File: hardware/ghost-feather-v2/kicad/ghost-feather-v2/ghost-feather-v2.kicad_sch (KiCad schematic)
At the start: 10 parts, among them U1 STM32F722RETx

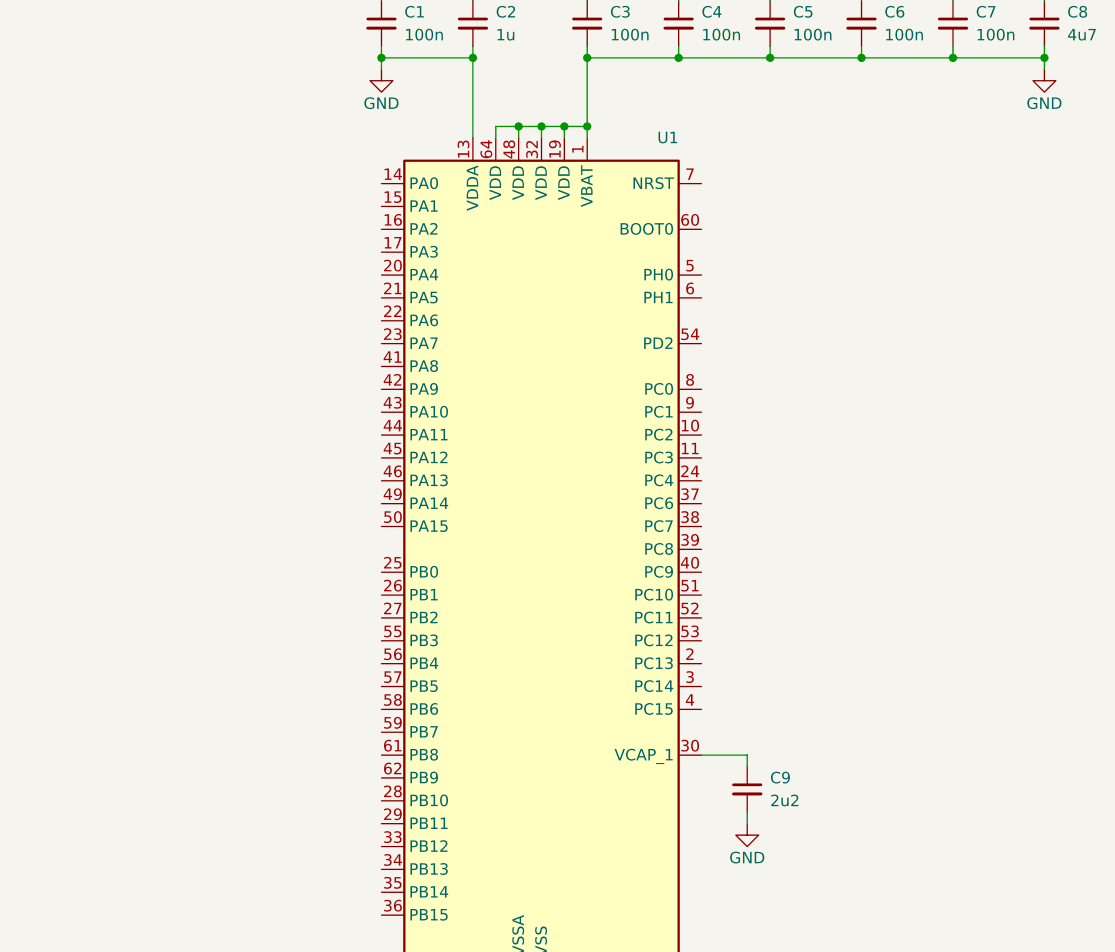
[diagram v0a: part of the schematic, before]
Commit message: feat: hardware: Add ghost-feather-v2 TAG Connector and user LED
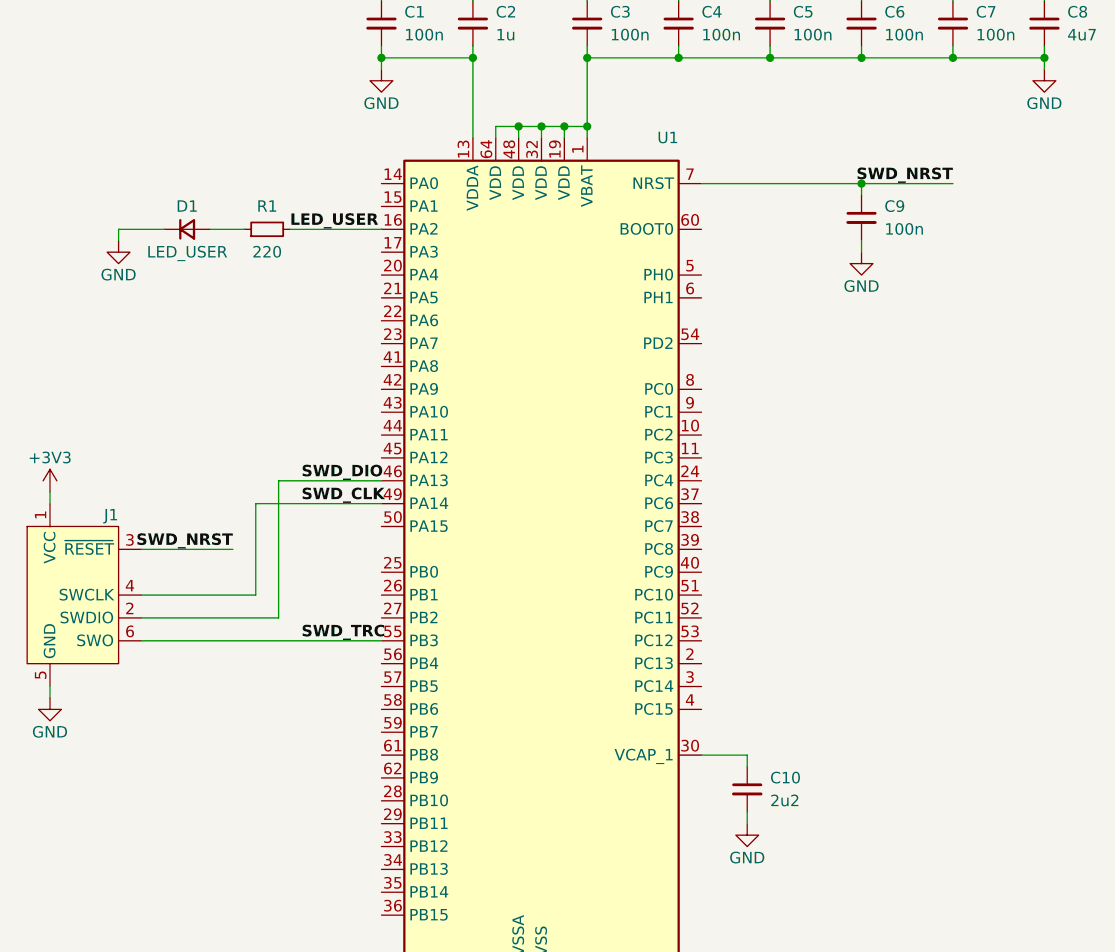
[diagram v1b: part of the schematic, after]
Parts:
- added C9: 100n, symbol Device:C_Small
- added D1: LED_USER, symbol Device:D_Small
- added J1: Conn_ARM_SWD_TagConnect_TC2030-NL, Connector:Tag-Connect_TC2030-IDC-NL_2x03_P1.27mm_Vertical, symbol Connector:Conn_ARM_SWD_TagConnect_TC2030-NL
- added R1: 220, symbol Device:R_Small
- renumbered C9 to C10
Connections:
- net +3V3: now also J1.1 (VCC)
- net GND: now also C9.2, D1.1 (K), J1.5 (GND)
- net LED_USER: now reaches U1.16 (PA2)
- net LED_USER: now also R1.2
- net SWD_DIO: now reaches U1.46 (PA13)
- net SWD_DIO: now also J1.2 (SWDIO)
- net SWD_CLK: now reaches U1.49 (PA14)
- net SWD_CLK: now also J1.4 (SWCLK)
- net SWD_TRC: now reaches U1.55 (PB3)
- net SWD_TRC: now also J1.6 (SWO)
- net SWD_NRST: now reaches U1.7 (NRST)
- net SWD_NRST: now also C9.1, J1.3 (~{RESET})
- new net: D1.2 (A), R1.1

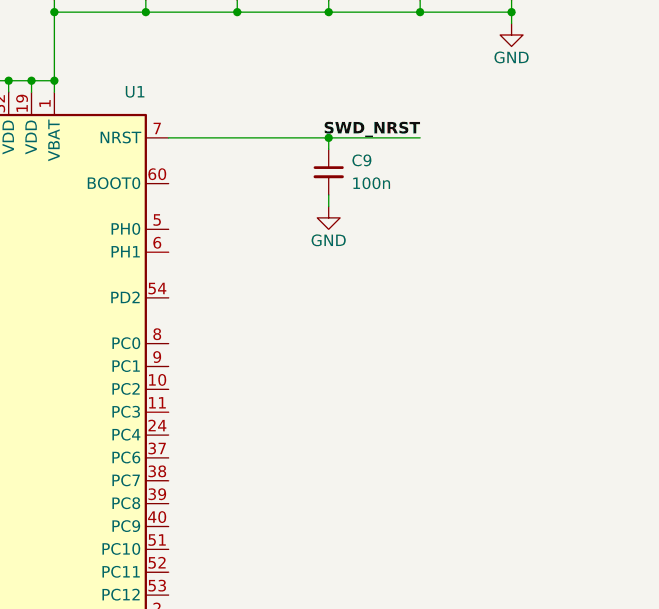
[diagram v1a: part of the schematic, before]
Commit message: feat: hardware: Add ghost-feather-v2 boot0 circuit
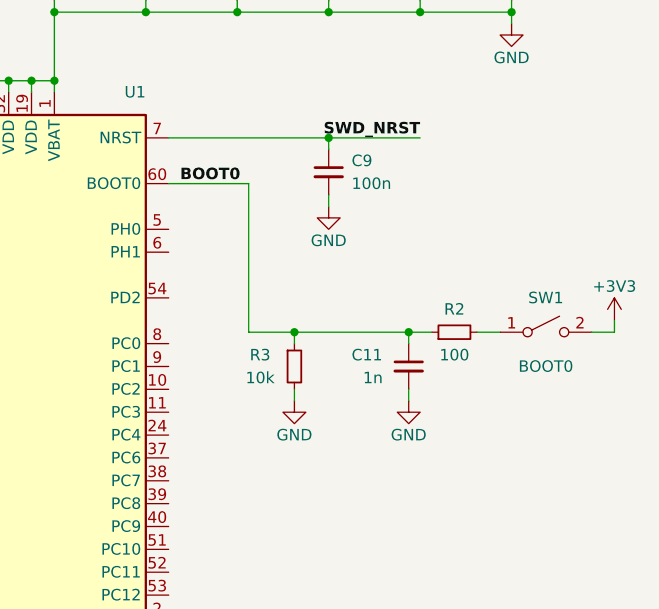
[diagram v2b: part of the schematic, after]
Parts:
- added C11: 1n, symbol Device:C_Small
- added R2: 100, symbol Device:R_Small
- added R3: 10k, symbol Device:R_Small
- added SW1: BOOT0, symbol Switch:SW_SPST
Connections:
- net +3V3: now also SW1.2 (B)
- net GND: now also C11.2, R3.2
- net BOOT0: now reaches U1.60 (BOOT0)
- net BOOT0: now also C11.1, R2.1, R3.1
- new net: R2.2, SW1.1 (A)
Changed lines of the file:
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@@
   (junction (at 186.69 53.34) (diameter 0) (color 0 0 0 0)
   )
+  (junction (at 195.58 74.93) (diameter 0) (color 0 0 0 0)
+  )
   (junction (at 143.51 39.37) (diameter 0) (color 0 0 0 0)
   )
@@
   (junction (at 133.35 39.37) (diameter 0) (color 0 0 0 0)
   )
+  (junction (at 182.88 74.93) (diameter 0) (color 0 0 0 0)
+  )
   (junction (at 151.13 46.99) (diameter 0) (color 0 0 0 0)
   )
@@
   (junction (at 148.59 143.51) (diameter 0) (color 0 0 0 0)
   )
+  (wire (pts (xy 195.58 81.28) (xy 195.58 82.55))
+    (stroke (width 0) (type default))
+  )
   (wire (pts (xy 207.01 30.48) (xy 207.01 31.75))
     (stroke (width 0) (type default))
@@
     (stroke (width 0) (type default))
   )
+  (wire (pts (xy 198.12 74.93) (xy 195.58 74.93))
+    (stroke (width 0) (type default))
+  )
+  (wire (pts (xy 182.88 74.93) (xy 177.8 74.93))
+    (stroke (width 0) (type default))
+  )
   (wire (pts (xy 168.91 116.84) (xy 173.99 116.84))
     (stroke (width 0) (type default))
@@
     (stroke (width 0) (type default))
   )
+  (wire (pts (xy 203.2 74.93) (xy 205.74 74.93))
+    (stroke (width 0) (type default))
+  )
   (wire (pts (xy 176.53 38.1) (xy 176.53 39.37))
     (stroke (width 0) (type default))
@@
     (stroke (width 0) (type default))
   )
+  (wire (pts (xy 215.9 74.93) (xy 218.44 74.93))
+    (stroke (width 0) (type default))
+  )
   (wire (pts (xy 156.21 31.75) (xy 166.37 31.75))
     (stroke (width 0) (type default))
@@
     (stroke (width 0) (type default))
   )
+  (wire (pts (xy 182.88 81.28) (xy 182.88 82.55))
+    (stroke (width 0) (type default))
+  )
+  (wire (pts (xy 168.91 58.42) (xy 177.8 58.42))
+    (stroke (width 0) (type default))
+  )
   (wire (pts (xy 151.13 142.24) (xy 151.13 143.51))
     (stroke (width 0) (type default))
@@
     (stroke (width 0) (type default))
   )
+  (wire (pts (xy 177.8 74.93) (xy 177.8 58.42))
+    (stroke (width 0) (type default))
+  )
   (wire (pts (xy 156.21 46.99) (xy 156.21 48.26))
     (stroke (width 0) (type default))
@@
     (stroke (width 0) (type default))
   )
+  (wire (pts (xy 218.44 73.66) (xy 218.44 74.93))
+    (stroke (width 0) (type default))
+  )
   (wire (pts (xy 133.35 88.9) (xy 119.38 88.9))
     (stroke (width 0) (type default))
@@
     (stroke (width 0) (type default))
   )
+  (wire (pts (xy 182.88 74.93) (xy 195.58 74.93))
+    (stroke (width 0) (type default))
+  )
   (wire (pts (xy 166.37 38.1) (xy 166.37 39.37))
     (stroke (width 0) (type default))
@@
   )
   (wire (pts (xy 153.67 46.99) (xy 156.21 46.99))
+    (stroke (width 0) (type default))
+  )
+  (wire (pts (xy 195.58 74.93) (xy 195.58 76.2))
+    (stroke (width 0) (type default))
+  )
+  (wire (pts (xy 182.88 74.93) (xy 182.88 76.2))
     (stroke (width 0) (type default))
   )
@@
   )
   (label "SWD_DIO" (at 124.46 86.36 0) (fields_autoplaced)
+    (effects (font (size 1.27 1.27) bold) (justify left bottom))
+  )
+  (label "BOOT0" (at 170.18 58.42 0) (fields_autoplaced)
     (effects (font (size 1.27 1.27) bold) (justify left bottom))
   )
@@
         (path "/f9a6fb30-e54e-4dec-8b48-0e9b06cf9ccb"
           (reference "C9") (unit 1)
+        )
+      )
+    )
+  )
+  (symbol (lib_id "Switch:SW_SPST") (at 210.82 74.93 0) (unit 1)
+    (in_bom yes) (on_board yes) (dnp no)
+    (property "Reference" "SW1" (at 210.82 71.12 0)
+      (effects (font (size 1.27 1.27)))
+    )
+    (property "Value" "BOOT0" (at 210.82 78.74 0)
+      (effects (font (size 1.27 1.27)))
+    )
+    (property "Footprint" "" (at 210.82 74.93 0)
+      (effects (font (size 1.27 1.27)) hide)
+    )
+    (property "Datasheet" "~" (at 210.82 74.93 0)
+      (effects (font (size 1.27 1.27)) hide)
+    )
+    (pin "1")
+    (pin "2")
+    (instances
+      (project "ghost-feather-v2"
+        (path "/f9a6fb30-e54e-4dec-8b48-0e9b06cf9ccb"
+          (reference "SW1") (unit 1)
         )
       )
@@
     )
   )
+  (symbol (lib_id "Device:R_Small") (at 200.66 74.93 90) (unit 1)
+    (in_bom yes) (on_board yes) (dnp no)
+    (property "Reference" "R2" (at 200.66 72.39 90)
+      (effects (font (size 1.27 1.27)))
+    )
+    (property "Value" "100" (at 200.66 77.47 90)
+      (effects (font (size 1.27 1.27)))
+    )
+    (property "Footprint" "" (at 200.66 74.93 0)
+      (effects (font (size 1.27 1.27)) hide)
+    )
+    (property "Datasheet" "~" (at 200.66 74.93 0)
+      (effects (font (size 1.27 1.27)) hide)
+    )
+    (pin "1")
+    (pin "2")
+    (instances
+      (project "ghost-feather-v2"
+        (path "/f9a6fb30-e54e-4dec-8b48-0e9b06cf9ccb"
+          (reference "R2") (unit 1)
+        )
+      )
+    )
+  )
   (symbol (lib_id "power:+3V3") (at 207.01 30.48 0) (unit 1)
     (in_bom yes) (on_board yes) (dnp no)
@@
         (path "/f9a6fb30-e54e-4dec-8b48-0e9b06cf9ccb"
           (reference "C3") (unit 1)
+        )
+      )
+    )
+  )
+  (symbol (lib_id "power:+3V3") (at 218.44 73.66 0) (unit 1)
+    (in_bom yes) (on_board yes) (dnp no)
+    (property "Reference" "#PWR011" (at 218.44 77.47 0)
+      (effects (font (size 1.27 1.27)) hide)
+    )
+    (property "Value" "+3V3" (at 218.44 69.85 0)
+      (effects (font (size 1.27 1.27)))
+    )
+    (property "Footprint" "" (at 218.44 73.66 0)
+      (effects (font (size 1.27 1.27)) hide)
+    )
+    (property "Datasheet" "" (at 218.44 73.66 0)
+      (effects (font (size 1.27 1.27)) hide)
+    )
+    (pin "1")
+    (instances
+      (project "ghost-feather-v2"
+        (path "/f9a6fb30-e54e-4dec-8b48-0e9b06cf9ccb"
+          (reference "#PWR011") (unit 1)
+        )
+      )
+    )
+  )
+  (symbol (lib_id "Device:C_Small") (at 195.58 78.74 0) (unit 1)
+    (in_bom yes) (on_board yes) (dnp no)
+    (property "Reference" "C11" (at 189.23 77.47 0)
+      (effects (font (size 1.27 1.27)) (justify left))
+    )
+    (property "Value" "1n" (at 190.5 80.01 0)
+      (effects (font (size 1.27 1.27)) (justify left))
+    )
+    (property "Footprint" "" (at 195.58 78.74 0)
+      (effects (font (size 1.27 1.27)) hide)
+    )
+    (property "Datasheet" "~" (at 195.58 78.74 0)
+      (effects (font (size 1.27 1.27)) hide)
+    )
+    (pin "1")
+    (pin "2")
+    (instances
+      (project "ghost-feather-v2"
+        (path "/f9a6fb30-e54e-4dec-8b48-0e9b06cf9ccb"
+          (reference "C11") (unit 1)
         )
       )
@@
         )
       )
+    )
+  )
+  (symbol (lib_id "power:GND") (at 195.58 82.55 0) (unit 1)
+    (in_bom yes) (on_board yes) (dnp no)
+    (property "Reference" "#PWR012" (at 195.58 88.9 0)
+      (effects (font (size 1.27 1.27)) hide)
+    )
+    (property "Value" "GND" (at 195.58 86.36 0)
+      (effects (font (size 1.27 1.27)))
+    )
+    (property "Footprint" "" (at 195.58 82.55 0)
+      (effects (font (size 1.27 1.27)) hide)
+    )
+    (property "Datasheet" "" (at 195.58 82.55 0)
+      (effects (font (size 1.27 1.27)) hide)
+    )
+    (pin "1")
+    (instances
+      (project "ghost-feather-v2"
+        (path "/f9a6fb30-e54e-4dec-8b48-0e9b06cf9ccb"
+          (reference "#PWR012") (unit 1)
+        )
+      )
+    )
+  )
+  (symbol (lib_id "power:GND") (at 182.88 82.55 0) (unit 1)
+    (in_bom yes) (on_board yes) (dnp no)
+    (property "Reference" "#PWR013" (at 182.88 88.9 0)
+      (effects (font (size 1.27 1.27)) hide)
+    )
+    (property "Value" "GND" (at 182.88 86.36 0)
+      (effects (font (size 1.27 1.27)))
+    )
+    (property "Footprint" "" (at 182.88 82.55 0)
+      (effects (font (size 1.27 1.27)) hide)
+    )
+    (property "Datasheet" "" (at 182.88 82.55 0)
+      (effects (font (size 1.27 1.27)) hide)
+    )
+    (pin "1")
+    (instances
+      (project "ghost-feather-v2"
+        (path "/f9a6fb30-e54e-4dec-8b48-0e9b06cf9ccb"
+          (reference "#PWR013") (unit 1)
+        )
+      )
+    )
+  )
+  (symbol (lib_id "Device:R_Small") (at 182.88 78.74 0) (unit 1)
+    (in_bom yes) (on_board yes) (dnp no)
+    (property "Reference" "R3" (at 179.07 77.47 0)
+      (effects (font (size 1.27 1.27)))
+    )
+    (property "Value" "10k" (at 179.07 80.01 0)
+      (effects (font (size 1.27 1.27)))
+    )
+    (property "Footprint" "" (at 182.88 78.74 0)
+      (effects (font (size 1.27 1.27)) hide)
+    )
+    (property "Datasheet" "~" (at 182.88 78.74 0)
+      (effects (font (size 1.27 1.27)) hide)
+    )
+    (pin "1")
+    (pin "2")
+    (instances
+      (project "ghost-feather-v2"
+        (path "/f9a6fb30-e54e-4dec-8b48-0e9b06cf9ccb"
+          (reference "R3") (unit 1)
+        )
+      )

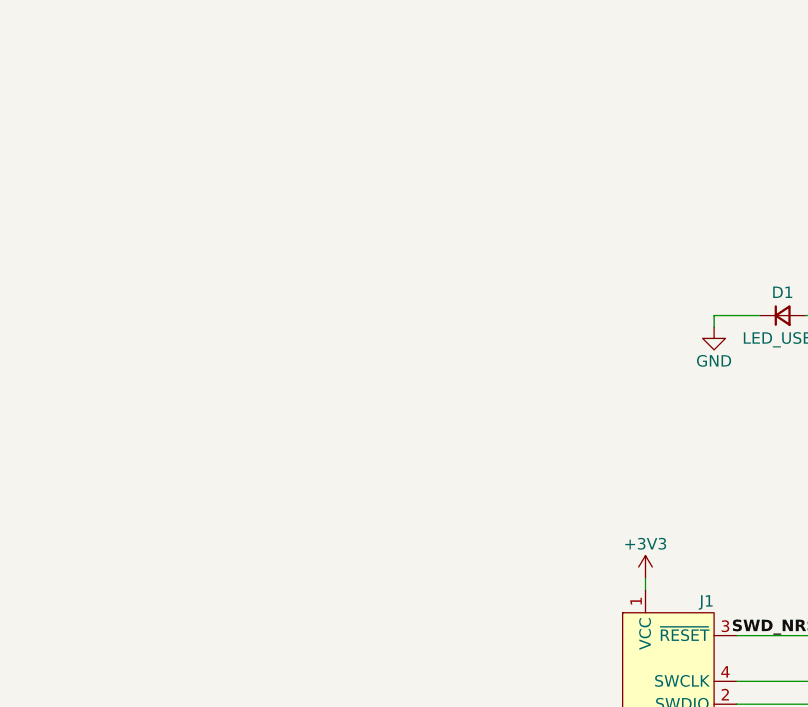
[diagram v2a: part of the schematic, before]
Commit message: feat: hardware: Add ghost-feather-v2 bmi088 sensor
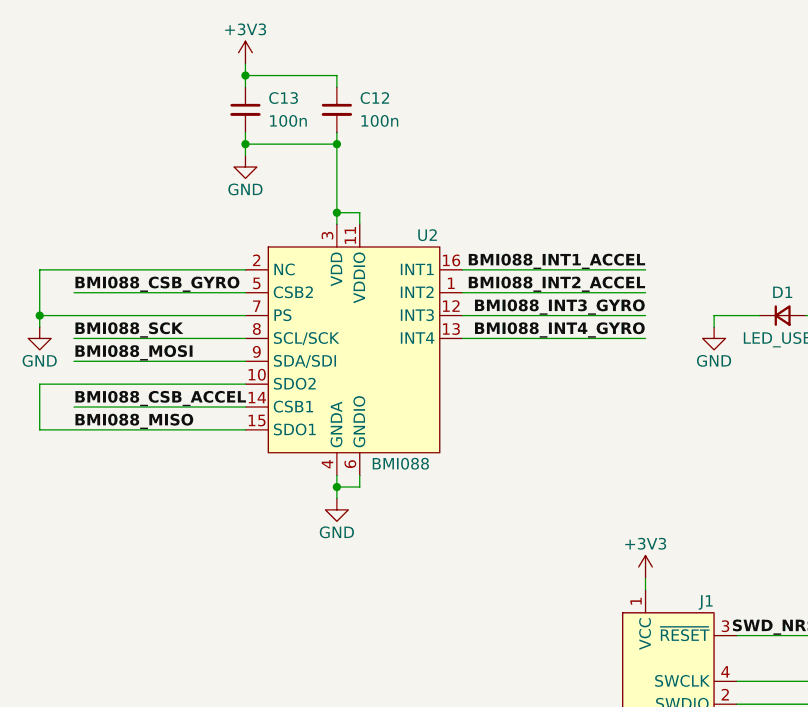
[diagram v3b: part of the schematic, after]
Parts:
- added C12, C13: 100n, symbol Device:C_Small
- added U2: BMI088, symbol Sensor_Motion:BMI088
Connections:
- net +3V3: now also C12.1, C13.1
- net GND: now also C12.2, C13.2, U2.11 (VDDIO), U2.2 (NC), U2.3 (VDD), U2.4 (GNDA), U2.6 (GNDIO), U2.7 (PS)
- new net BMI088_CSB_ACCEL: U2.14 (CSB1)
- new net BMI088_CSB_GYRO: U2.5 (CSB2)
- new net BMI088_INT1_ACCEL: U2.16 (INT1)
- new net BMI088_INT2_ACCEL: U2.1 (INT2)
- new net BMI088_INT3_GYRO: U2.12 (INT3)
- new net BMI088_INT4_GYRO: U2.13 (INT4)
- new net BMI088_MISO: U2.10 (SDO2), U2.15 (SDO1)
- new net BMI088_MOSI: U2.9 (SDA/SDI)
- new net BMI088_SCK: U2.8 (SCL/SCK)
